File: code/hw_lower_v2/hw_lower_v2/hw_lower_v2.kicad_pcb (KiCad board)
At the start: 4 copper layers, 101.5 x 106 mm, 114 parts, among them J1 Screw_Terminal_01x01, J10 Conn_01x02, J11 Conn_01x02, J12 Conn_01x02, J13 Conn_01x02, J14 Conn_01x02, J2 Screw_Terminal_01x01, J3 Screw_Terminal_01x01, J4 Screw_Terminal_01x01, J5 Screw_Terminal_01x01, J6 Screw_Terminal_01x01, J7 Conn_01x06_Pin, J8 Conn_02x20_Odd_Even, J9 Conn_01x02, K1 AHES4191, Q1 BSS138, Q2 BSS138, Q3 BSS138, T1 TS3193-2C 2mA/2mA, U1 BRCS02C, U2 BL0942, U3 DRV8220DRL, U4 TLV1805, U5 ICL7660A, U6 AMS1117, U7 AMS1117

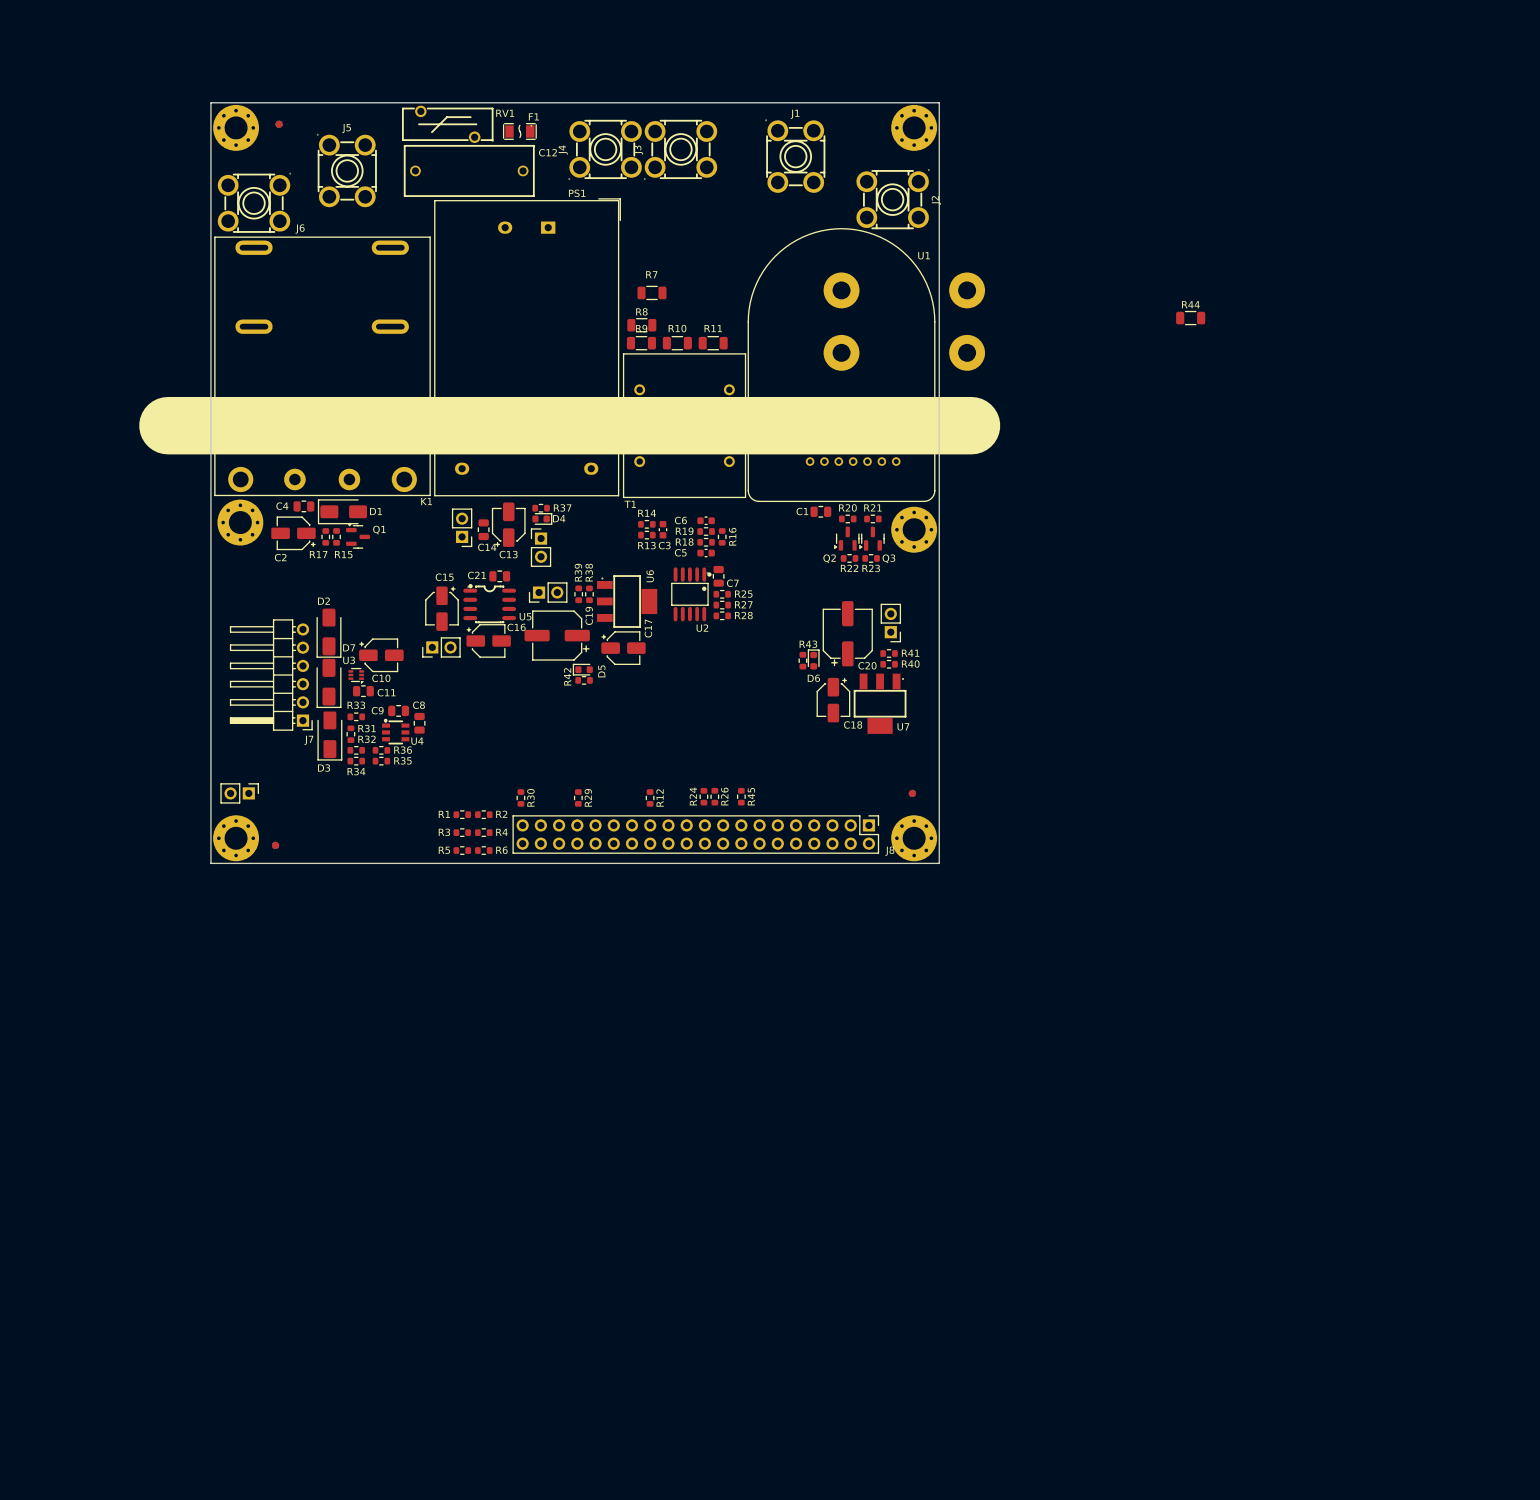
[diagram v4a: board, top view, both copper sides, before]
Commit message: further placement and pin relocation
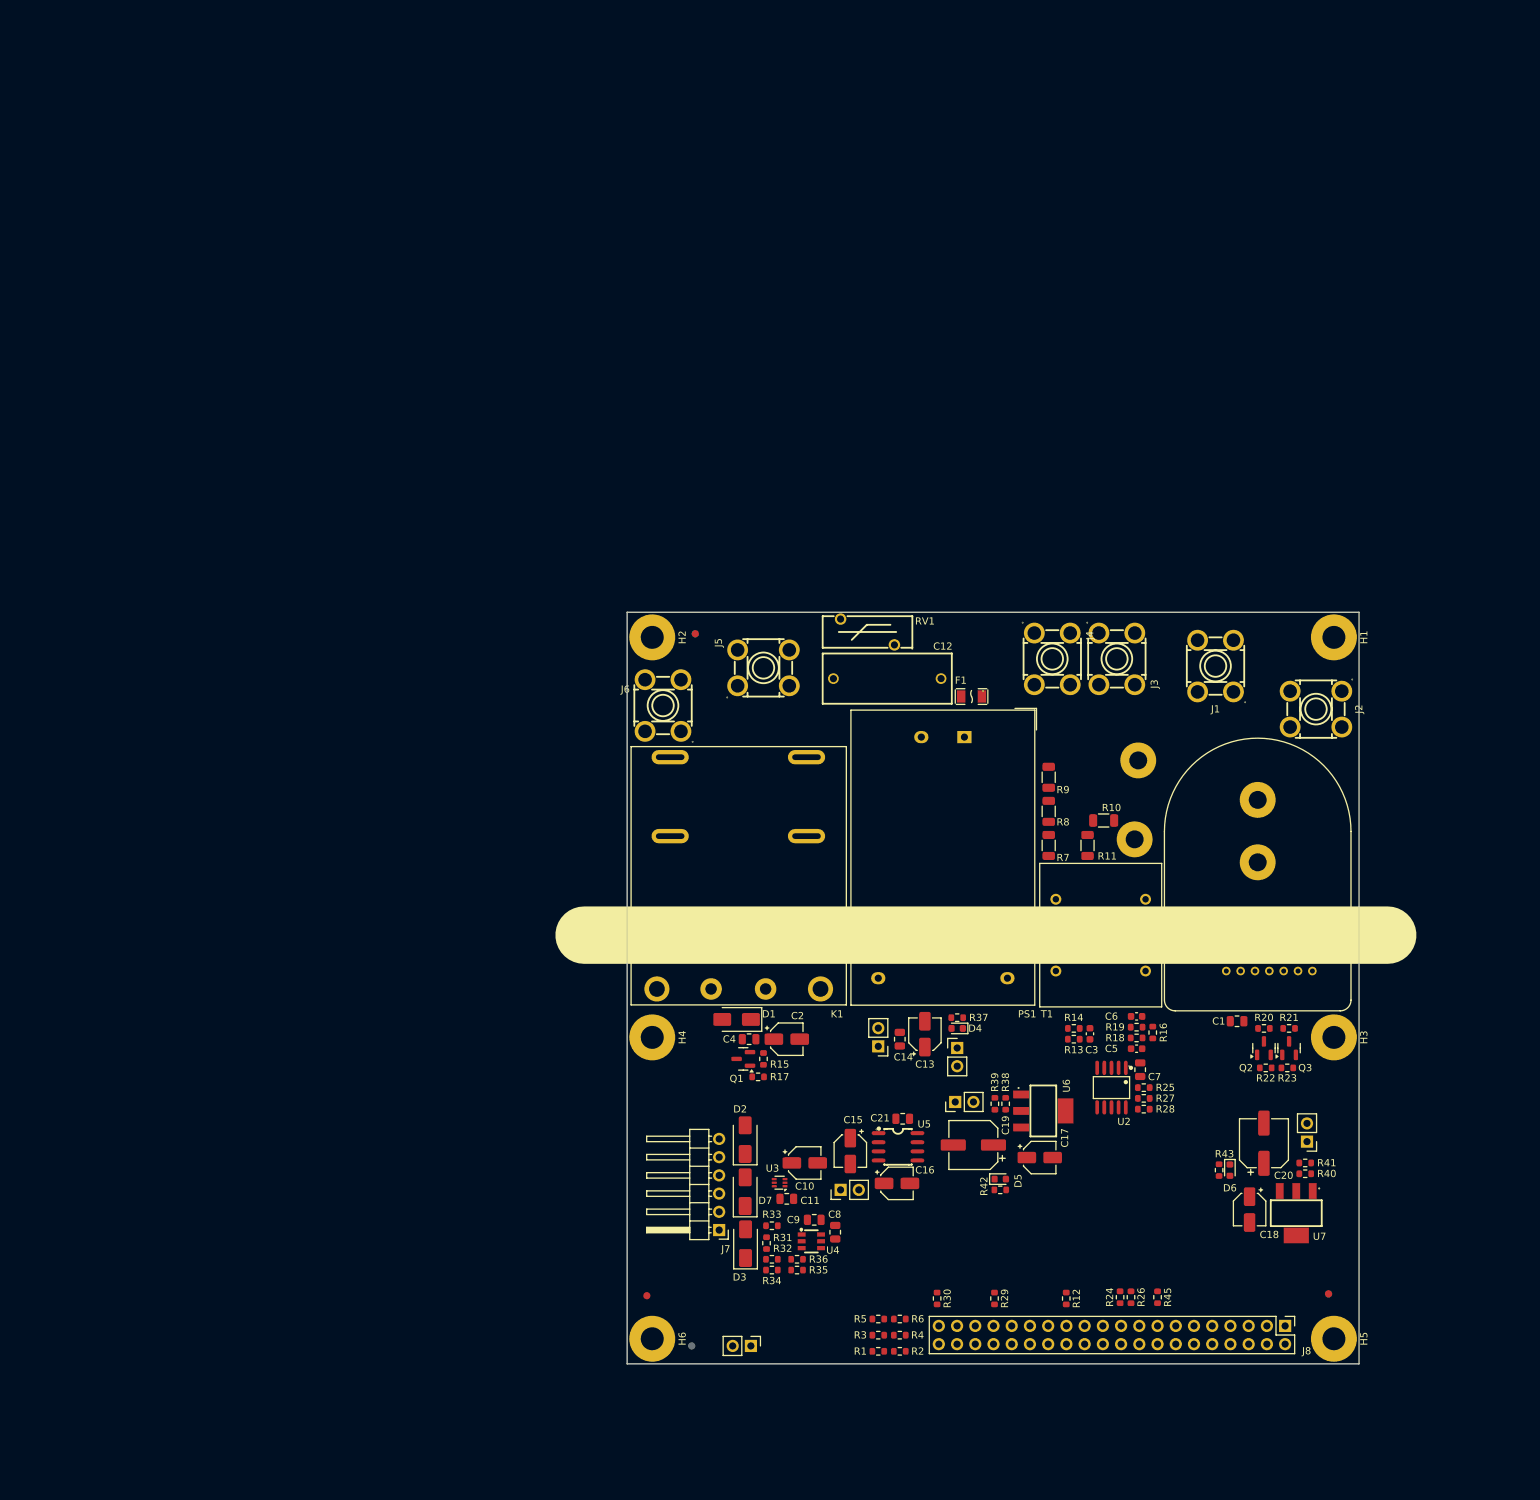
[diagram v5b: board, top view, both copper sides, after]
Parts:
- removed R44: 1M, Resistor_SMD:R_1206_3216Metric
- H1, H2, H3, H4, H5, H6: value MountingHole_Pad -> MountingHole; footprint MountingHole:MountingHole_3.2mm_M3_Pad_Via -> MountingHole:MountingHole_3.2mm_M3_Pad
- U1: footprint multi_new:BRCS02C_1 -> multi_new:BRCS02C_2
- moved J14 104.0 mm to (117.2, 202.2)
- moved F1 100.8 mm to (148.0, 111.8)
- moved C2 98.5 mm to (122.2, 159.5), turned to 0 degrees
- moved C4 96.8 mm to (117.0, 159.5)
- moved R17 96.4 mm to (118.2, 164.8), turned to 180 degrees
- moved R7 94.8 mm to (158.8, 132.5), turned to -90 degrees
- moved R1 94.6 mm to (135.0, 203.0)
- moved R2 94.6 mm to (138.0, 203.0)
- moved C15 94.6 mm to (131.1, 175.1)
- moved C16 94.6 mm to (137.6, 179.6)
- moved J11 94.6 mm to (129.8, 180.5)
- moved U5 94.6 mm to (137.8, 174.5)
- moved J4 94.4 mm to (159.2, 106.5), turned to 0 degrees
- moved C21 94.2 mm to (138.4, 170.6)
- moved R15 94.0 mm to (119.0, 162.2), turned to -90 degrees
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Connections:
- C12 pad 2: /AC/N_in -> /AC/N_internal_power
- F1 pad 1: /AC/L_in -> /AC/L_internal_power
- H1 pad 1: unconnected-(H1-Pad1) -> (no net)
- H2 pad 1: unconnected-(H2-Pad1) -> (no net)
- H3 pad 1: unconnected-(H3-Pad1) -> (no net)
- H4 pad 1: unconnected-(H4-Pad1) -> (no net)
- H5 pad 1: unconnected-(H5-Pad1) -> (no net)
- H6 pad 1: unconnected-(H6-Pad1) -> (no net)
- K1 pad 1: Net-(D1-A) -> +12V
- K1 pad 2: +12V -> Net-(D1-A)
- K1 pad 3: GND -> /AC/AC_RELAY_SENSE
- K1 pad 4: /AC/AC_RELAY_SENSE -> GND
- K1 pad 5: /AC/L_out -> /AC/N_internal_power
- K1 pad 6: Net-(K1-Pad6) -> /AC/N_out
- K1 pad 7: /AC/N_out -> /AC/L_internal_power
- K1 pad 8: Net-(K1-Pad8) -> /AC/L_out
- PS1 pad 2: /AC/N_in -> /AC/N_internal_power
- R10 pad 2: Net-(R10-Pad2) -> /AC/N_internal_power
- R7 pad 2: Net-(R7-Pad2) -> Net-(T1-AB)
- R8 pad 1: /AC/N_in -> Net-(R8-Pad1)
- R9 pad 1: Net-(R10-Pad2) -> /AC/L_internal_power
- R9 pad 2: Net-(R7-Pad2) -> Net-(R8-Pad1)
- RV1 pad 2: /AC/N_in -> /AC/N_internal_power
- T1 pad 2: /AC/L_in -> Net-(T1-AB)
- U1 pad 10: /AC/L_in -> /AC/N_in
- U1 pad 11: Net-(K1-Pad6) -> /AC/N_internal_power
- U1 pad 8: /AC/N_in -> /AC/L_in
- U1 pad 9: Net-(K1-Pad8) -> /AC/L_internal_power
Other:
- board size 101.5 x 106 mm -> 102 x 104.8 mm

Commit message: commit before experimenting
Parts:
- H1, H2: footprint MountingHole:MountingHole_3.2mm_M3_Pad -> MountingHole:MountingHole_3.2mm_M3
- moved FID2 82.2 mm to (191.8, 103.0)
- moved FID4 82.2 mm to (191.8, 103.0)
- moved C17 13.5 mm to (144.0, 176.2), turned to -90 degrees
- moved U6 10.4 mm to (150.5, 176.8), turned to 90 degrees
- moved C15 8.12 mm to (130.5, 167.0)
- moved C16 8.12 mm to (137.0, 171.5)
- moved C8 8.12 mm to (128.4, 178.3)
- moved D2 8.12 mm to (115.8, 165.4)
- moved D7 8.12 mm to (115.8, 172.7)
- moved J11 8.12 mm to (129.1, 172.4)
- moved U5 8.12 mm to (137.1, 166.4)
- moved C10 8.12 mm to (124.1, 168.7)
- moved C11 8.12 mm to (121.6, 173.7)
- moved C21 8.12 mm to (137.8, 162.5)
- moved C9 8.12 mm to (125.5, 176.6)
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
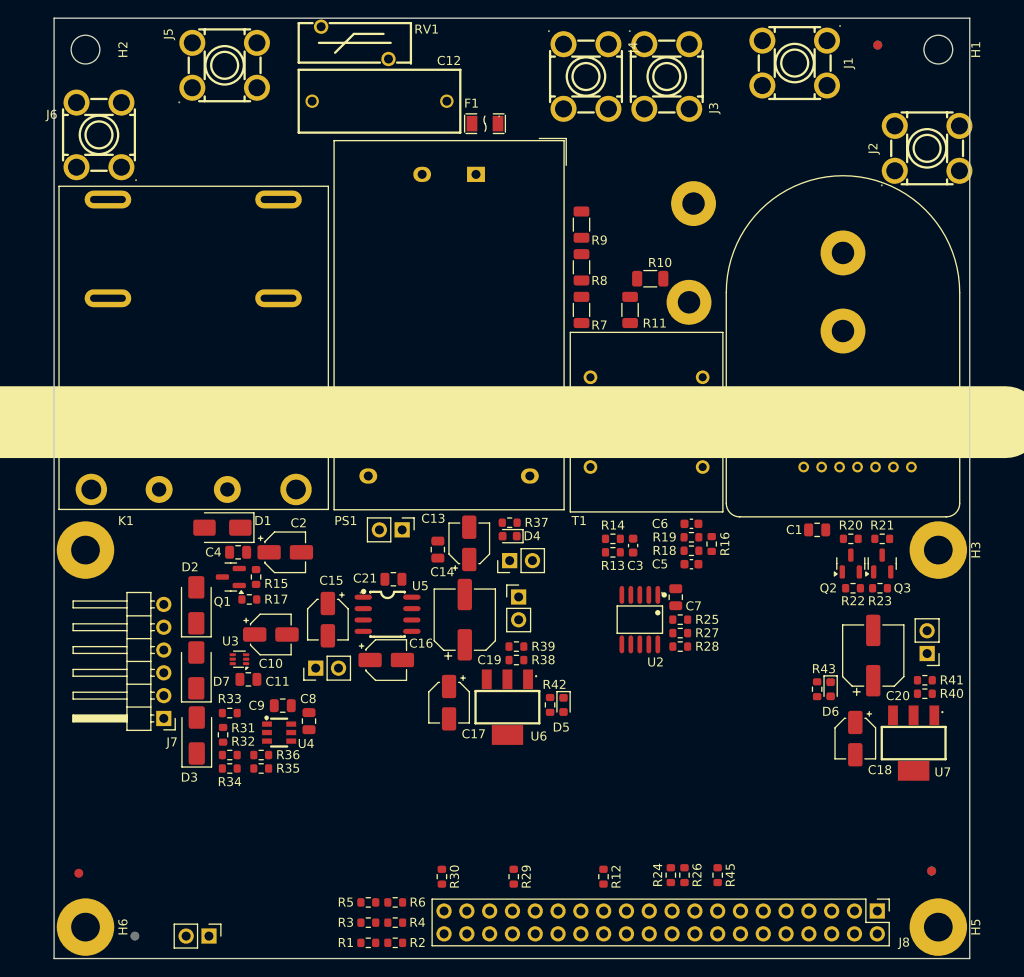
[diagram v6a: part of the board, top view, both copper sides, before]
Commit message: switch power  pin headers for jumpers
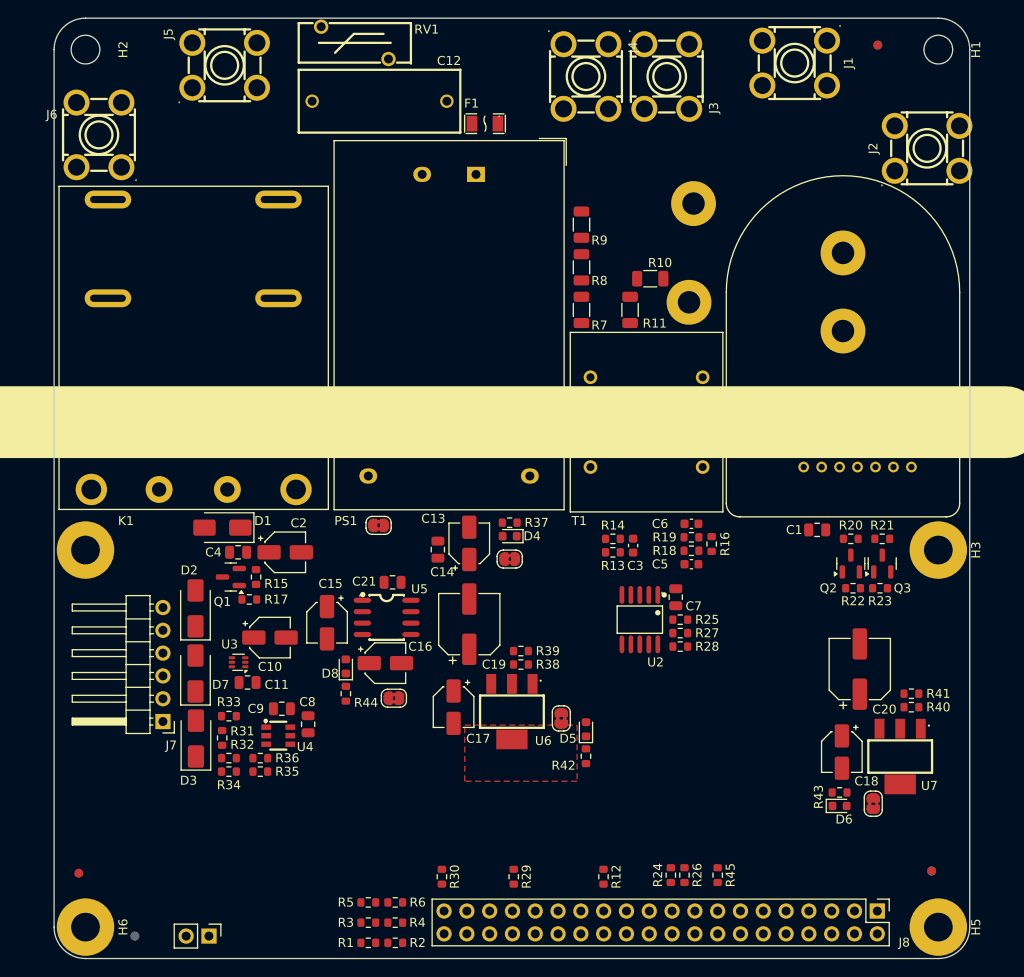
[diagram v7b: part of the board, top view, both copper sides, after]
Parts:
- removed J10, J11, J12, J13, J9: Conn_01x02, Connector_PinHeader_2.54mm:PinHeader_1x02_P2.54mm_Vertical
- added D8: RED LED, Diode_SMD:D_0603_1608Metric, F.Cu at (132.5, 172.2)
- added JP1: SolderJumper_2_Bridged, Jumper:SolderJumper-2_P1.3mm_Bridged2Bar_RoundedPad1.0x1.5mm, F.Cu at (150.8, 160.2)
- added JP2: SolderJumper_2_Bridged, Jumper:SolderJumper-2_P1.3mm_Bridged2Bar_RoundedPad1.0x1.5mm, F.Cu at (136.2, 156.5)
- added JP3: SolderJumper_2_Bridged, Jumper:SolderJumper-2_P1.3mm_Bridged2Bar_RoundedPad1.0x1.5mm, F.Cu at (137.8, 175.8)
- added JP4: SolderJumper_2_Bridged, Jumper:SolderJumper-2_P1.3mm_Bridged2Bar_RoundedPad1.0x1.5mm, F.Cu at (156.5, 178.0)
- added JP5: SolderJumper_2_Bridged, Jumper:SolderJumper-2_P1.3mm_Bridged2Bar_RoundedPad1.0x1.5mm, F.Cu at (191.2, 187.5)
- added R44: 510R, Resistor_SMD:R_0603_1608Metric, F.Cu at (132.5, 175.2)
- moved D6 13.0 mm to (187.5, 187.8), turned to 0 degrees
- moved R43 11.8 mm to (187.5, 186.2), turned to 0 degrees
- moved R42 6.97 mm to (159.2, 182.2)
- moved D5 3.69 mm to (159.2, 179.2), turned to 90 degrees
- moved C18 2.12 mm to (187.8, 181.8)
- moved C20 2.12 mm to (189.8, 172.5)
- moved R40 2.12 mm to (195.5, 176.8)
- moved R41 2.12 mm to (195.5, 175.2)
- moved U7 2.12 mm to (194.2, 182.2)
- moved C17 0.71 mm to (144.5, 176.8)
- moved C19 0.71 mm to (146.2, 167.5)
- moved R38 0.71 mm to (152.0, 172.0)
- moved R39 0.71 mm to (152.0, 170.5)
- moved U6 0.71 mm to (151.0, 177.2)
- moved C10 0.36 mm to (124.0, 169.0)
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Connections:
- C13 pad 1: +12V -> Net-(JP1-B)
- C14 pad 1: +12V -> Net-(JP1-B)
- C16 pad 2: -12V -> Net-(JP3-B)
- C19 pad 1: +3.3V -> Net-(JP4-B)
- C20 pad 1: +5V -> Net-(JP5-B)
- PS1 pad 4: +12V -> Net-(JP2-B)
- R38 pad 2: +3.3V -> Net-(JP4-B)
- R40 pad 2: +5V -> Net-(JP5-B)
- U5 pad 5: -12V -> Net-(JP3-B)
- U6 pad 2: +3.3V -> Net-(JP4-B)
- U7 pad 2: +5V -> Net-(JP5-B)
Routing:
- added copper zone on F.Cu, net +3.3V
- added copper zone on In1.Cu, net GND
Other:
- outline, holes or cut-outs redrawn

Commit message: have one project part library
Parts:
- C12: footprint JLCPCB:CAP-TH_L18.0-W7.0-P15.00-D0.7 -> multi_new:CAP-TH_L18.0-W7.0-P15.00-D0.7
- F1: footprint JLCPCB:F1206 -> multi_new:F1206
- J1, J2, J3, J4, J5, J6: footprint JLCPCB:CONN-TH_T44001 -> multi_new:CONN-TH_T44001
- RV1: footprint JLCPCB:RES-TH_L12.5-W4.4-P7.50-D0.8-S3.60 -> multi_new:RES-TH_L12.5-W4.4-P7.50-D0.8-S3.60
- U2: footprint JLCPCB:SSOP-10_L4.9-W3.9-P1.00-LS6.0-BL -> multi_new:SSOP-10_L4.9-W3.9-P1.00-LS6.0-BL
- U4: footprint JLCPCB:SOT-23-6_L2.9-W1.6-P0.95-LS2.8-BR -> multi_new:SOT-23-6_L2.9-W1.6-P0.95-LS2.8-BR
- U5: footprint JLCPCB:SOIC-8_L5.0-W4.0-P1.27-LS6.0-BL -> multi_new:SOIC-8_L5.0-W4.0-P1.27-LS6.0-BL
- U6, U7: footprint JLCPCB:SOT-223_L6.7-W3.5-P2.30-BR -> multi_new:SOT-223_L6.7-W3.5-P2.30-BR
- moved J14 72.9 mm to (188.5, 217.7), turned to 0 degrees
- moved C7 1.60 mm to (170.5, 163.5)
- moved R25 1.60 mm to (171.0, 166.0)
- moved R27 1.60 mm to (171.0, 167.5)
- moved R28 1.60 mm to (171.0, 169.0)
- moved U2 1.60 mm to (166.5, 166.0)
- moved J2 1.25 mm to (196.2, 113.8)
- moved C3 0.35 mm to (164.8, 158.5)
- moved R13 0.35 mm to (162.5, 157.8)
- moved R14 0.35 mm to (162.5, 159.2)
- moved C5 0.07 mm to (171.0, 160.8)
- moved C6 0.07 mm to (171.0, 156.2)
- moved R16 0.07 mm to (173.2, 158.5)
- moved R18 0.07 mm to (171.0, 159.2)
- moved R19 0.07 mm to (171.0, 157.8)
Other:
- board text added: "fillet: 3.5mm"
- board text removed: "1"
